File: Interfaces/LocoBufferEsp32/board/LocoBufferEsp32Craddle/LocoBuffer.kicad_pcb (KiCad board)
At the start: 4 copper layers, 75 x 50 mm, 23 parts, among them J2 RJ12, J3 RJ12, Q1 SS8050, Q2 SS8050, U1 LM311, U5 ESP32-DevKitC

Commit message: Mejoras Cradle
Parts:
- added J1: Conn_01x04, Connector_PinHeader_2.54mm:PinHeader_1x04_P2.54mm_Vertical, F.Cu at (100.2, 86.9)
- moved U5 50.2 mm to (90.7, 117.4), turned to 180 degrees
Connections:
- U5 pad 10: unconnected-(U5-DAC_2/ADC2_CH9/GPIO26-Pad10) -> /SDA
- U5 pad 11: unconnected-(U5-ADC2_CH7/GPIO27-Pad11) -> /SCL
- U5 pad 36: /LnTx -> /LnRx
- U5 pad 37: /LnRx -> /LnTx
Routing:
- net /LnTx: track 76.2 -> 34.9 mm
- net /LnRx: track 89.1 -> 69.1 mm
- net /SDA: track 0.00 -> 9.55 mm
- net /SCL: track 0.00 -> 9.55 mm

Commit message: LocoCradle
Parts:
- added C1: 22 uF, Capacitor_SMD:C_1206_3216Metric, F.Cu at (50.8, 76.5)
- added C2: 22 uF, Capacitor_SMD:C_1206_3216Metric, F.Cu at (58.8, 91.9)
- added D3: SS24A, Diode_SMD:D_SMA, F.Cu at (53.2, 90.4)
- added D4: SS24A, Diode_SMD:D_SMA, F.Cu at (53.2, 94.6)
- added D5: SS24A, Diode_SMD:D_SMA, F.Cu at (59.2, 78.1)
- added D6: LED, LED_SMD:LED_0805_2012Metric, F.Cu at (43.4, 74.3)
- added D7: LED, LED_SMD:LED_0805_2012Metric, F.Cu at (45.7, 74.3)
- added R12: 470, Resistor_SMD:R_0805_2012Metric, F.Cu at (43.4, 78.7)
- added R13: 470, Resistor_SMD:R_0805_2012Metric, F.Cu at (45.7, 78.7)
- added U2: AMS1117-5.0, Package_TO_SOT_SMD:SOT-223-3_TabPin2, F.Cu at (52.9, 82.9)
- moved R1 20.3 mm to (53.5, 110.1)
- moved Q2 20.3 mm to (52.8, 115.6)
- moved R10 20.3 mm to (56.7, 114.6)
- moved R11 20.3 mm to (56.7, 116.6)
- moved R2 20.3 mm to (53.5, 112.1)
- moved R3 20.3 mm to (60.3, 103.7)
- moved R4 20.3 mm to (53.5, 108.1)
- moved R5 20.3 mm to (53.4, 106.0)
- moved R7 20.3 mm to (60.3, 105.7)
- moved U1 20.3 mm to (60.4, 110.1)
- moved D2 3.67 mm to (43.7, 116.0)
- moved R8 3.67 mm to (43.7, 112.1)
- moved D1 3.67 mm to (41.0, 116.1)
- moved Q1 3.67 mm to (47.1, 116.1)
- moved R6 3.67 mm to (41.0, 112.2)
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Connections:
- net Net-(J2-Pad1) renamed /LocoNet/RSyncA
- net Net-(J2-Pad6) renamed /LocoNet/RSyncB
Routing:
- net +5V: track 0.00 -> 36.8 mm
- net /LnPower5V: track 0.00 -> 23.6 mm
- net /LnRx: track 69.1 -> 50.9 mm
- net /LnPower: track 0.00 -> 15.1 mm
- net /LocoNet/RSyncB: track 16.8 -> 29.2 mm
- net /LocoNet/RSyncA: track 16.1 -> 25.2 mm
- net /LocoNet/loconet: track 46.7 -> 55.2 mm
- net /LnTx: track 34.9 -> 29.2 mm
- net Net-(D7-A): track 0.00 -> 2.60 mm
- net Net-(D6-A): track 0.00 -> 2.59 mm
- net /SDA: track 9.55 -> 7.54 mm
- net /SCL: track 9.55 -> 7.54 mm
- net +3.3V: track 9.84 -> 11.3 mm, vias 3 -> 5
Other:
- board text added: "LnT"
- board text added: "Pwr"

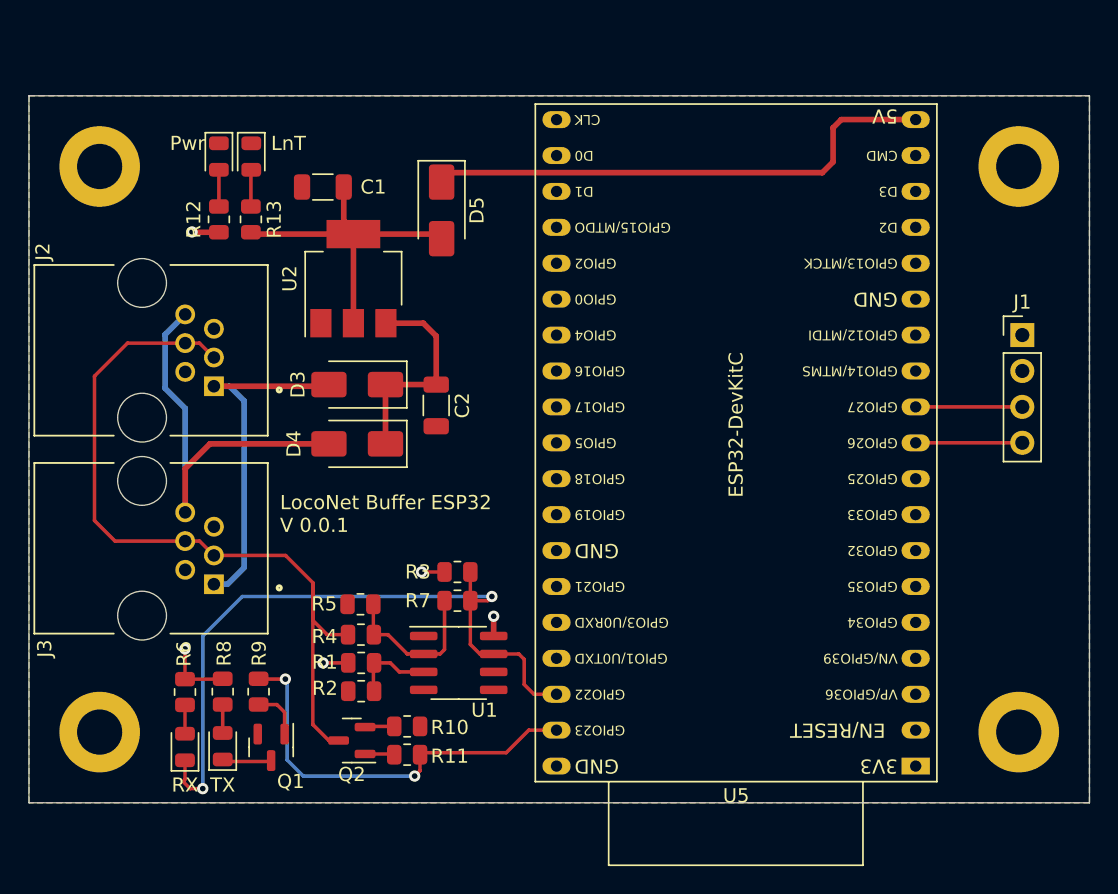
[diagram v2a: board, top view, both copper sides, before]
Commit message: Btn and RGB Led
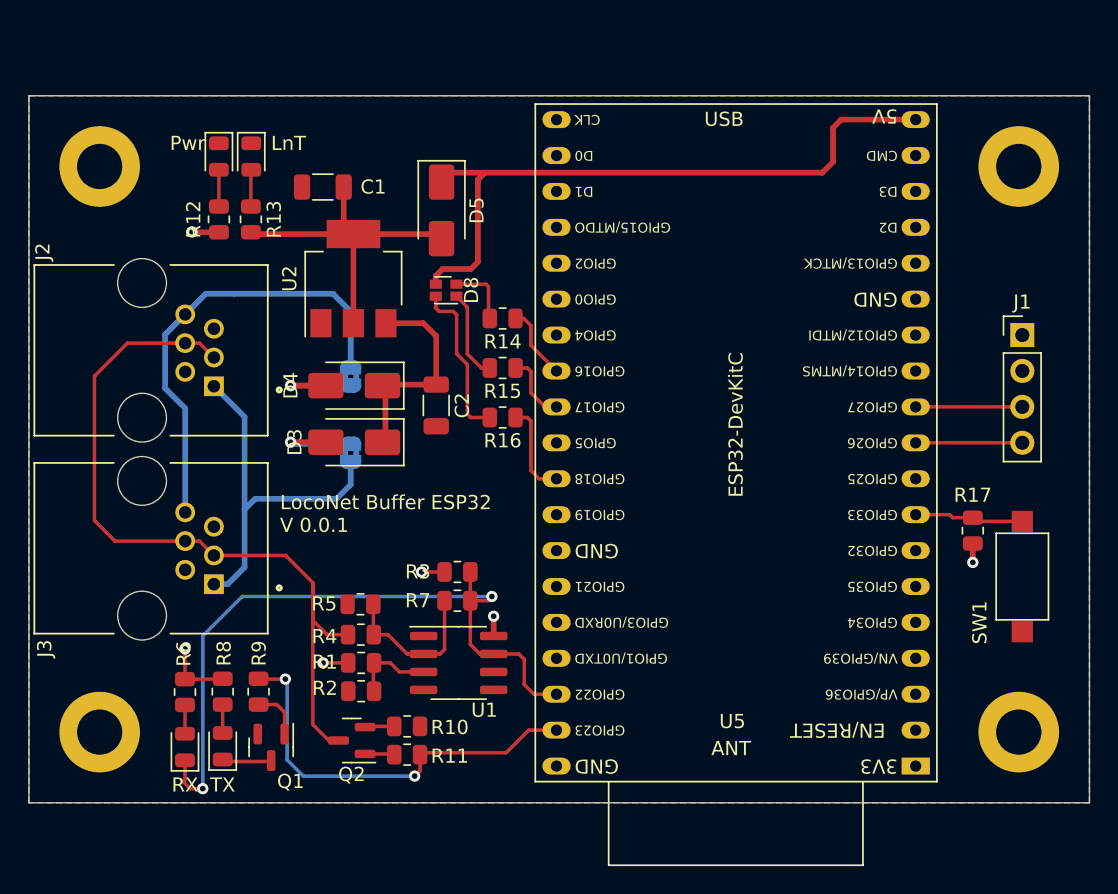
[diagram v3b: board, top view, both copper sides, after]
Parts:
- added D8: LTST-C19HE1WT, LED_SMD:LED_LiteOn_LTST-C19HE1WT, F.Cu at (59.5, 83.8)
- added JP1: SolderJumper_2_Bridged, Jumper:SolderJumper-2_P1.3mm_Bridged2Bar_RoundedPad1.0x1.5mm, B.Cu at (52.8, 95.2)
- added JP2: SolderJumper_2_Bridged, Jumper:SolderJumper-2_P1.3mm_Bridged2Bar_RoundedPad1.0x1.5mm, B.Cu at (52.8, 89.8)
- added R14: 470, Resistor_SMD:R_0805_2012Metric, F.Cu at (63.5, 85.8)
- added R15: 470, Resistor_SMD:R_0805_2012Metric, F.Cu at (63.5, 89.2)
- added R16: 470, Resistor_SMD:R_0805_2012Metric, F.Cu at (63.5, 92.8)
- added R17: 10K (5%), Resistor_SMD:R_0805_2012Metric, F.Cu at (96.8, 100.8)
- added SW1: SW_Push, Button_Switch_SMD:SW_SPST_CK_RS282G05A3, F.Cu at (100.2, 104.0)
- moved D4 4.12 mm to (53.0, 90.5)
- moved D3 4.08 mm to (53.0, 94.5)
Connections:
- D3 pad 2: /LocoNet/RSyncA -> /RSyncAC
- D4 pad 2: /LocoNet/RSyncB -> /RSyncBC
- U5 pad 12: unconnected-(U5-MTMS/GPIO14/ADC2_CH6-Pad12) -> /HSPI_SCLK
- U5 pad 13: unconnected-(U5-MTDI/GPIO12/ADC2_CH5-Pad13) -> /HSPI_MISO
- U5 pad 15: unconnected-(U5-MTCK/GPIO13/ADC2_CH4-Pad15) -> /HSPI_MOSI
- U5 pad 23: unconnected-(U5-MTDO/GPIO15/ADC2_CH3-Pad23) -> /HSPI_CS
- U5 pad 27: unconnected-(U5-GPIO16-Pad27) -> /LedR
- U5 pad 28: unconnected-(U5-GPIO17-Pad28) -> /LedG
- U5 pad 30: unconnected-(U5-GPIO18-Pad30) -> /LedB
- U5 pad 8: unconnected-(U5-32K_XN/GPIO33/ADC1_CH5-Pad8) -> /btnLb
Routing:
- net Net-(D8-BK): track 0.00 -> 11.5 mm
- net +5V: track 36.8 -> 47.3 mm
- net /btnLb: track 0.00 -> 8.24 mm
- net /RSyncBC: track 0.00 -> 7.02 mm, vias 0 -> 1
- net /RSyncAC: track 0.00 -> 6.79 mm, vias 0 -> 1
- net /LedB: track 0.00 -> 6.74 mm
- net Net-(D8-GK): track 0.00 -> 6.40 mm
- net /LedR: track 0.00 -> 5.26 mm
- net /LedG: track 0.00 -> 4.92 mm
- net Net-(D8-RK): track 0.00 -> 4.63 mm
- net /LocoNet/RSyncB: track 29.2 -> 32.0 mm
- net +3.3V: track 11.3 -> 12.7 mm, vias 5 -> 6
- net /LocoNet/RSyncA: track 25.2 -> 26.2 mm
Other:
- board text added: "ANT"
- board text added: "USB"
